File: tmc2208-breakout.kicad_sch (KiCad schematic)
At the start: 41 parts, among them J1 Conn_01x05, J2 Conn_01x05, J3 Conn_01x04, J4 Conn_01x02, U1 TMC2208-LA

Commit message: changed some minor things like connector and finalized bom for v1.0
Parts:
- removed J1, J2: Conn_01x05, Connector_PinHeader_2.54mm:PinHeader_1x05_P2.54mm_Vertical, symbol Connector_Generic:Conn_01x05
- added J1: Conn_01x11, Connector_PinHeader_2.54mm:PinHeader_1x11_P2.54mm_Vertical, symbol Connector_Generic:Conn_01x11
- C7: footprint Capacitor_SMD:CP_Elec_5x5.4 -> Capacitor_SMD:CP_Elec_6.3x5.4
- FID1, FID2, H1, H2, H3, H4, TP12, TP14, TP15, TP16, TP18, TP19, TP20: now left out of the parts list
- R8: value R -> 0
- TP1: value TestPoint -> EN#; now left out of the parts list
- TP2: value TestPoint -> DIR; now left out of the parts list
- TP3: value TestPoint -> MS1; now left out of the parts list
- TP4: value TestPoint -> MS2; now left out of the parts list
- TP5: value TestPoint -> STEP; now left out of the parts list
- TP6: value TestPoint -> DIAG; now left out of the parts list
- TP7: value TestPoint -> INDX; now left out of the parts list
- TP8: value TestPoint -> PDN; now left out of the parts list
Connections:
- net +3V3: now also J1.11 (Pin_11)
- net DIAG: now also J1.7 (Pin_7)
- net DIR: now also J1.1 (Pin_1)
- net EN#: now also J1.4 (Pin_4)
- net GND: now also J1.10 (Pin_10)
- net INDEX: now also J1.8 (Pin_8)
- net MS1: now also J1.5 (Pin_5)
- net MS2: now also J1.6 (Pin_6)
- net PDN_UART: now also J1.9 (Pin_9)
- net STEP: now also J1.3 (Pin_3)
- net VREF: now also J1.2 (Pin_2)

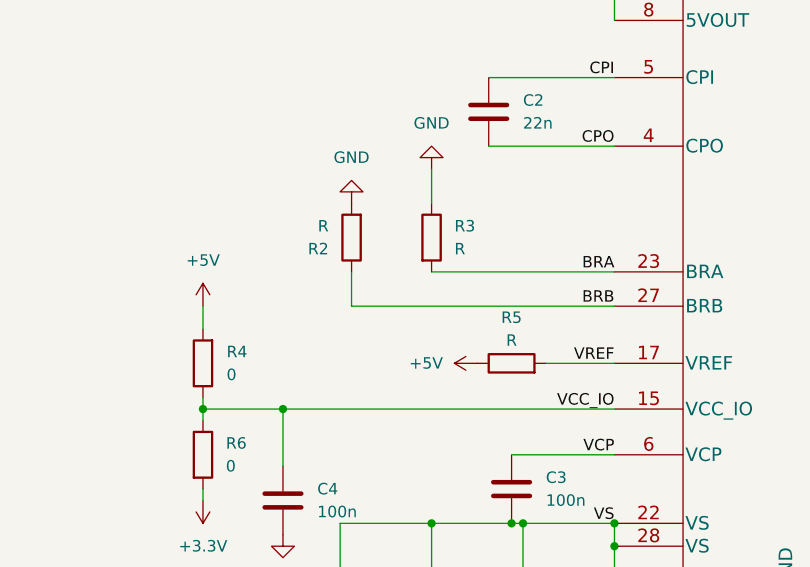
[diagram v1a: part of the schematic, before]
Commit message: added lcsc field to components for ibom, also changed r5 to 33k
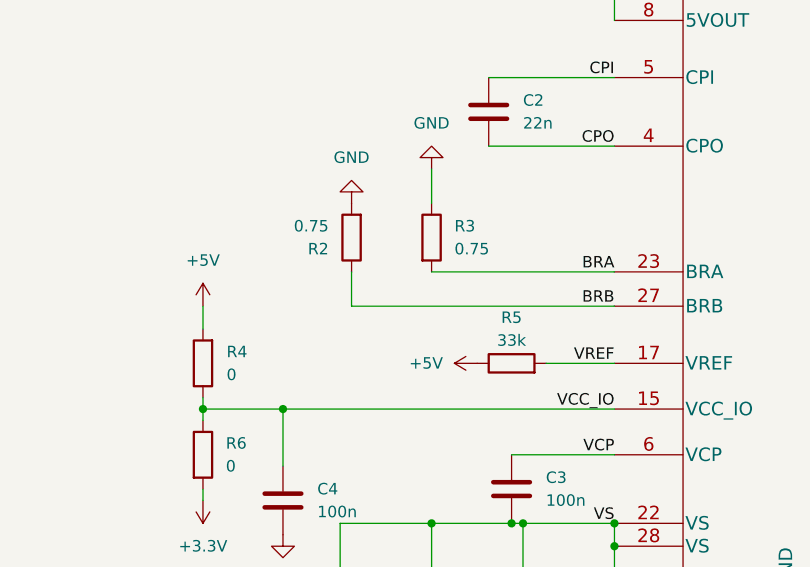
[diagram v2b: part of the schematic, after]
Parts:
- C1: LCSC (none) -> C23630
- C2: LCSC (none) -> C106222
- C3, C4, C5, C6: LCSC (none) -> C1591
- C7: LCSC (none) -> C129250
- J1: LCSC (none) -> C429959
- J3: LCSC (none) -> C144395
- J4: LCSC (none) -> C8404
- R1, R4, R6, R7, R8: LCSC (none) -> C100044
- R2, R3: value R -> 0.75; LCSC (none) -> C175689
- R5: value R -> 33k; LCSC (none) -> C25593
- U1: LCSC (none) -> C115944
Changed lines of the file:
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@@
+      (effects (font (size 1.27 1.27)) hide)
+    )
+    (property "LCSC" "C100044" (id 4) (at 69.85 118.11 0)
       (effects (font (size 1.27 1.27)) hide)
     )
@@
     )
     (property "Datasheet" "~" (id 3) (at 247.65 100.33 0)
+      (effects (font (size 1.27 1.27)) hide)
+    )
+    (property "LCSC" "C429959" (id 4) (at 247.65 100.33 0)
       (effects (font (size 1.27 1.27)) hide)
     )
@@
       (effects (font (size 1.27 1.27)) hide)
     )
+    (property "LCSC" "C8404" (id 4) (at 247.65 130.81 0)
+      (effects (font (size 1.27 1.27)) hide)
+    )
     (pin "1")
     (pin "2")
@@
     (in_bom yes) (on_board yes)
     (property "Reference" "R5" (id 0) (at 104.14 102.87 90))
-    (property "Value" "R" (id 1) (at 104.14 105.41 90))
+    (property "Value" "33k" (id 1) (at 104.14 105.41 90))
     (property "Footprint" "Resistor_SMD:R_0603_1608Metric_Pad0.98x0.95mm_HandSolder" (id 2) (at 104.14 109.728 90)
       (effects (font (size 1.27 1.27)) hide)
     )
     (property "Datasheet" "~" (id 3) (at 104.14 107.95 0)
+      (effects (font (size 1.27 1.27)) hide)
+    )
+    (property "LCSC" "C25593" (id 4) (at 104.14 107.95 0)
       (effects (font (size 1.27 1.27)) hide)
     )
@@
       (effects (font (size 1.27 1.27)) (justify left))
     )
-    (property "Value" "R" (id 1) (at 83.82 92.7101 0)
+    (property "Value" "0.75" (id 1) (at 83.82 92.7101 0)
       (effects (font (size 1.27 1.27)) (justify left))
     )
@@
       (effects (font (size 1.27 1.27)) hide)
     )
+    (property "LCSC" "C175689" (id 4) (at 86.36 93.98 0)
+      (effects (font (size 1.27 1.27)) hide)
+    )
     (pin "1")
     (pin "2")
@@
     )
     (property "Datasheet" "~" (id 3) (at 104.14 121.92 0)
+      (effects (font (size 1.27 1.27)) hide)
+    )
+    (property "LCSC" "C1591" (id 4) (at 104.14 121.92 0)
       (effects (font (size 1.27 1.27)) hide)
     )
@@
       (effects (font (size 1.27 1.27)) hide)
     )
+    (property "LCSC" "C144395" (id 4) (at 247.65 120.65 0)
+      (effects (font (size 1.27 1.27)) hide)
+    )
     (pin "1")
     (pin "2")
@@
       (effects (font (size 1.27 1.27)) (justify left))
     )
-    (property "Value" "R" (id 1) (at 97.79 95.2499 0)
+    (property "Value" "0.75" (id 1) (at 97.79 95.2499 0)
       (effects (font (size 1.27 1.27)) (justify left))
     )
@@
     )
     (property "Datasheet" "~" (id 3) (at 95.25 93.98 0)
+      (effects (font (size 1.27 1.27)) hide)
+    )
+    (property "LCSC" "C175689" (id 4) (at 95.25 93.98 0)
       (effects (font (size 1.27 1.27)) hide)
     )
@@
     )
     (property "Datasheet" "~" (id 3) (at 78.74 123.19 0)
+      (effects (font (size 1.27 1.27)) hide)
+    )
+    (property "LCSC" "C1591" (id 4) (at 78.74 123.19 0)
       (effects (font (size 1.27 1.27)) hide)
     )
@@
       (effects (font (size 1.27 1.27)) hide)
     )
+    (property "LCSC" "C129250" (id 4) (at 115.57 135.89 0)
+      (effects (font (size 1.27 1.27)) hide)
+    )
     (pin "1")
     (pin "2")
@@
       (effects (font (size 1.27 1.27)) hide)
     )
+    (property "LCSC" "C1591" (id 4) (at 95.25 135.89 0)
+      (effects (font (size 1.27 1.27)) hide)
+    )
     (pin "1")
     (pin "2")
@@
       (effects (font (size 1.27 1.27)) hide)
     )
+    (property "LCSC" "C100044" (id 4) (at 85.09 135.89 0)
+      (effects (font (size 1.27 1.27)) hide)
+    )
     (pin "1")
     (pin "2")
@@
     )
     (property "Datasheet" "~" (id 3) (at 109.22 54.61 0)
+      (effects (font (size 1.27 1.27)) hide)
+    )
+    (property "LCSC" "C23630" (id 4) (at 109.22 54.61 0)
       (effects (font (size 1.27 1.27)) hide)
     )
@@
       (effects (font (size 1.27 1.27)) hide)
     )
+    (property "LCSC" "C100044" (id 4) (at 173.99 129.54 0)
+      (effects (font (size 1.27 1.27)) hide)
+    )
     (pin "1")
     (pin "2")
@@
       (effects (font (size 1.27 1.27)) hide)
     )
+    (property "LCSC" "C100044" (id 4) (at 69.85 107.95 0)
+      (effects (font (size 1.27 1.27)) hide)
+    )
     (pin "1")
     (pin "2")
@@
       (effects (font (size 1.27 1.27)) hide)
     )
+    (property "LCSC" "C100044" (id 4) (at 173.99 63.5 0)
+      (effects (font (size 1.27 1.27)) hide)
+    )
     (pin "1")
     (pin "2")
@@
     )
     (property "Datasheet" "~" (id 3) (at 101.6 80.01 0)
+      (effects (font (size 1.27 1.27)) hide)
+    )
+    (property "LCSC" "C106222" (id 4) (at 101.6 80.01 0)
       (effects (font (size 1.27 1.27)) hide)
     )
@@
     (property "Datasheet" "" (id 3) (at 115.57 72.39 0)
       (effects (font (size 1.524 1.524)))
+    )
+    (property "LCSC" "C115944" (id 4) (at 115.57 72.39 0)
+      (effects (font (size 1.27 1.27)) hide)
     )
     (pin "1")
@@
       (effects (font (size 1.27 1.27)) hide)
     )
+    (property "LCSC" "C1591" (id 4) (at 105.41 135.89 0)
+      (effects (font (size 1.27 1.27)) hide)
+    )
     (pin "1")
     (pin "2")
@@
     )
     (path "/35647c0b-a712-4bcf-bfe4-7afc232d5443"
-      (reference "R2") (unit 1) (value "R") (footprint "Resistor_SMD:R_0603_1608Metric_Pad0.98x0.95mm_HandSolder")
+      (reference "R2") (unit 1) (value "0.75") (footprint "Resistor_SMD:R_0603_1608Metric_Pad0.98x0.95mm_HandSolder")
     )
     (path "/57e27ea6-8287-4886-b181-17584a91c0ad"
-      (reference "R3") (unit 1) (value "R") (footprint "Resistor_SMD:R_0603_1608Metric_Pad0.98x0.95mm_HandSolder")
+      (reference "R3") (unit 1) (value "0.75") (footprint "Resistor_SMD:R_0603_1608Metric_Pad0.98x0.95mm_HandSolder")
     )
     (path "/c1614fe9-c7db-4327-9506-6ec6a21f9dea"
@@
     )
     (path "/2e7a88c5-edd4-45c4-84ff-0681783ee835"
-      (reference "R5") (unit 1) (value "R") (footprint "Resistor_SMD:R_0603_1608Metric_Pad0.98x0.95mm_HandSolder")
+      (reference "R5") (unit 1) (value "33k") (footprint "Resistor_SMD:R_0603_1608Metric_Pad0.98x0.95mm_HandSolder")
     )
     (path "/02b76a02-ea34-48c0-8406-5d90b64f6d97"

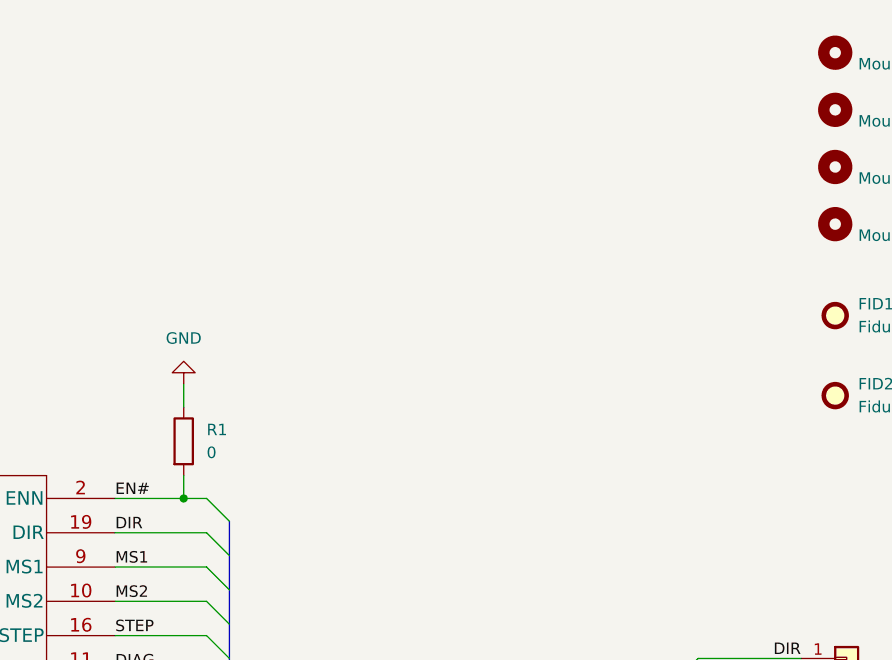
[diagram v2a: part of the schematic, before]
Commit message: added LEDs for EN# and STEP
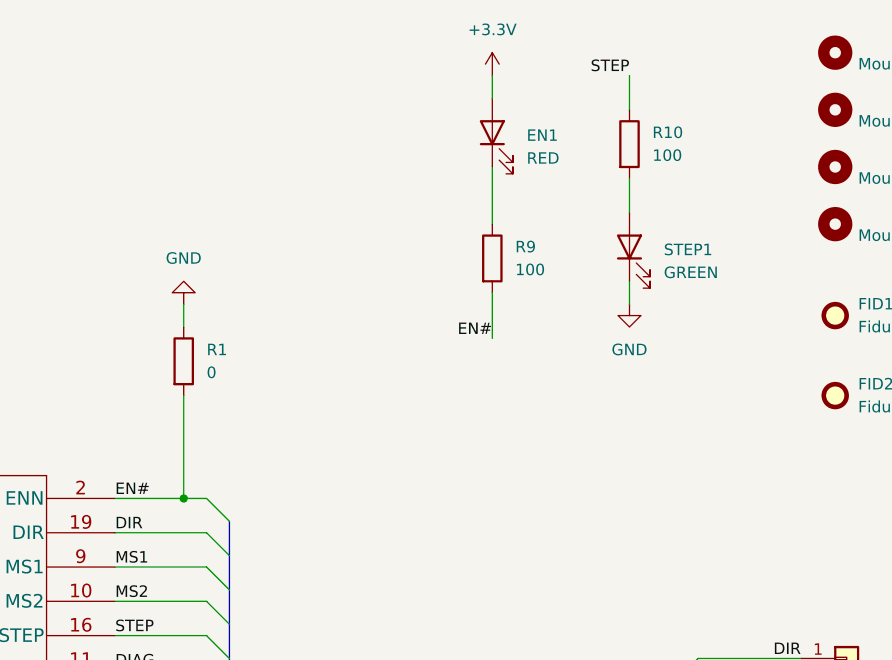
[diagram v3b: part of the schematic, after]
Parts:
- added EN1: RED, LED_SMD:LED_1206_3216Metric_Pad1.42x1.75mm_HandSolder, symbol Device:LED
- added R10, R9: 100, Resistor_SMD:R_0603_1608Metric_Pad0.98x0.95mm_HandSolder, symbol Device:R
- added STEP1: GREEN, LED_SMD:LED_1206_3216Metric_Pad1.42x1.75mm_HandSolder, symbol Device:LED
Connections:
- net +3V3: now also EN1.2 (A)
- net EN#: now also R9.2
- net GND: now also STEP1.1 (K)
- net STEP: now also R10.1
- new net: EN1.1 (K), R9.1
- new net: R10.2, STEP1.2 (A)
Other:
- moved on the sheet: R1
